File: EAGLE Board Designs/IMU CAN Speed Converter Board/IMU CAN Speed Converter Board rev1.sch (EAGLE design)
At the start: 24 parts, among them J1 CONNECTOR-CAN_NF_S_RA_BLACK, J2 CONNECTOR-CAN_NF_S_RA_BLACK, J3 JUMPER_1X02_, J4 JUMPER_1X02_, U1 LM340, U2 TCAN1051HQV-Q1, U3 TCAN1051HQV-Q1

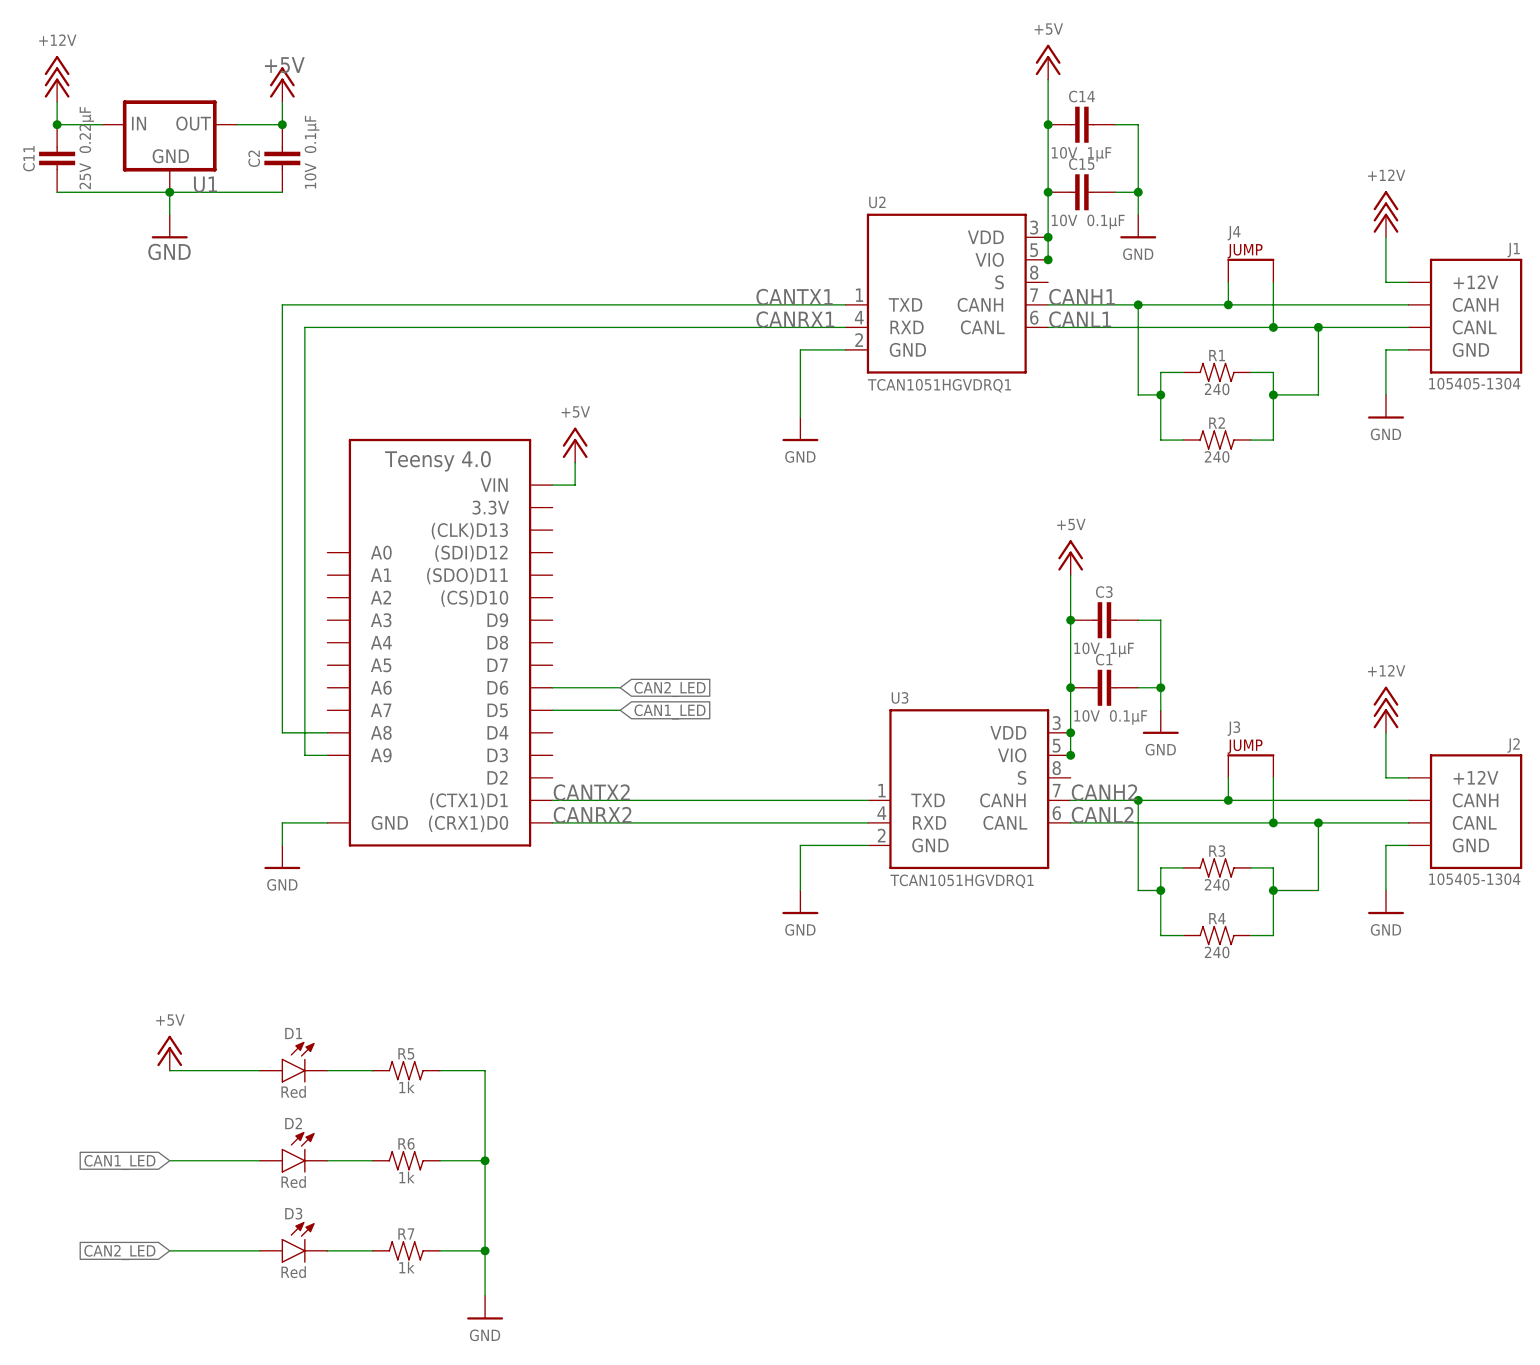
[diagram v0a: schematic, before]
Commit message: Update IMU CAN Speed Converter Board rev1.sch
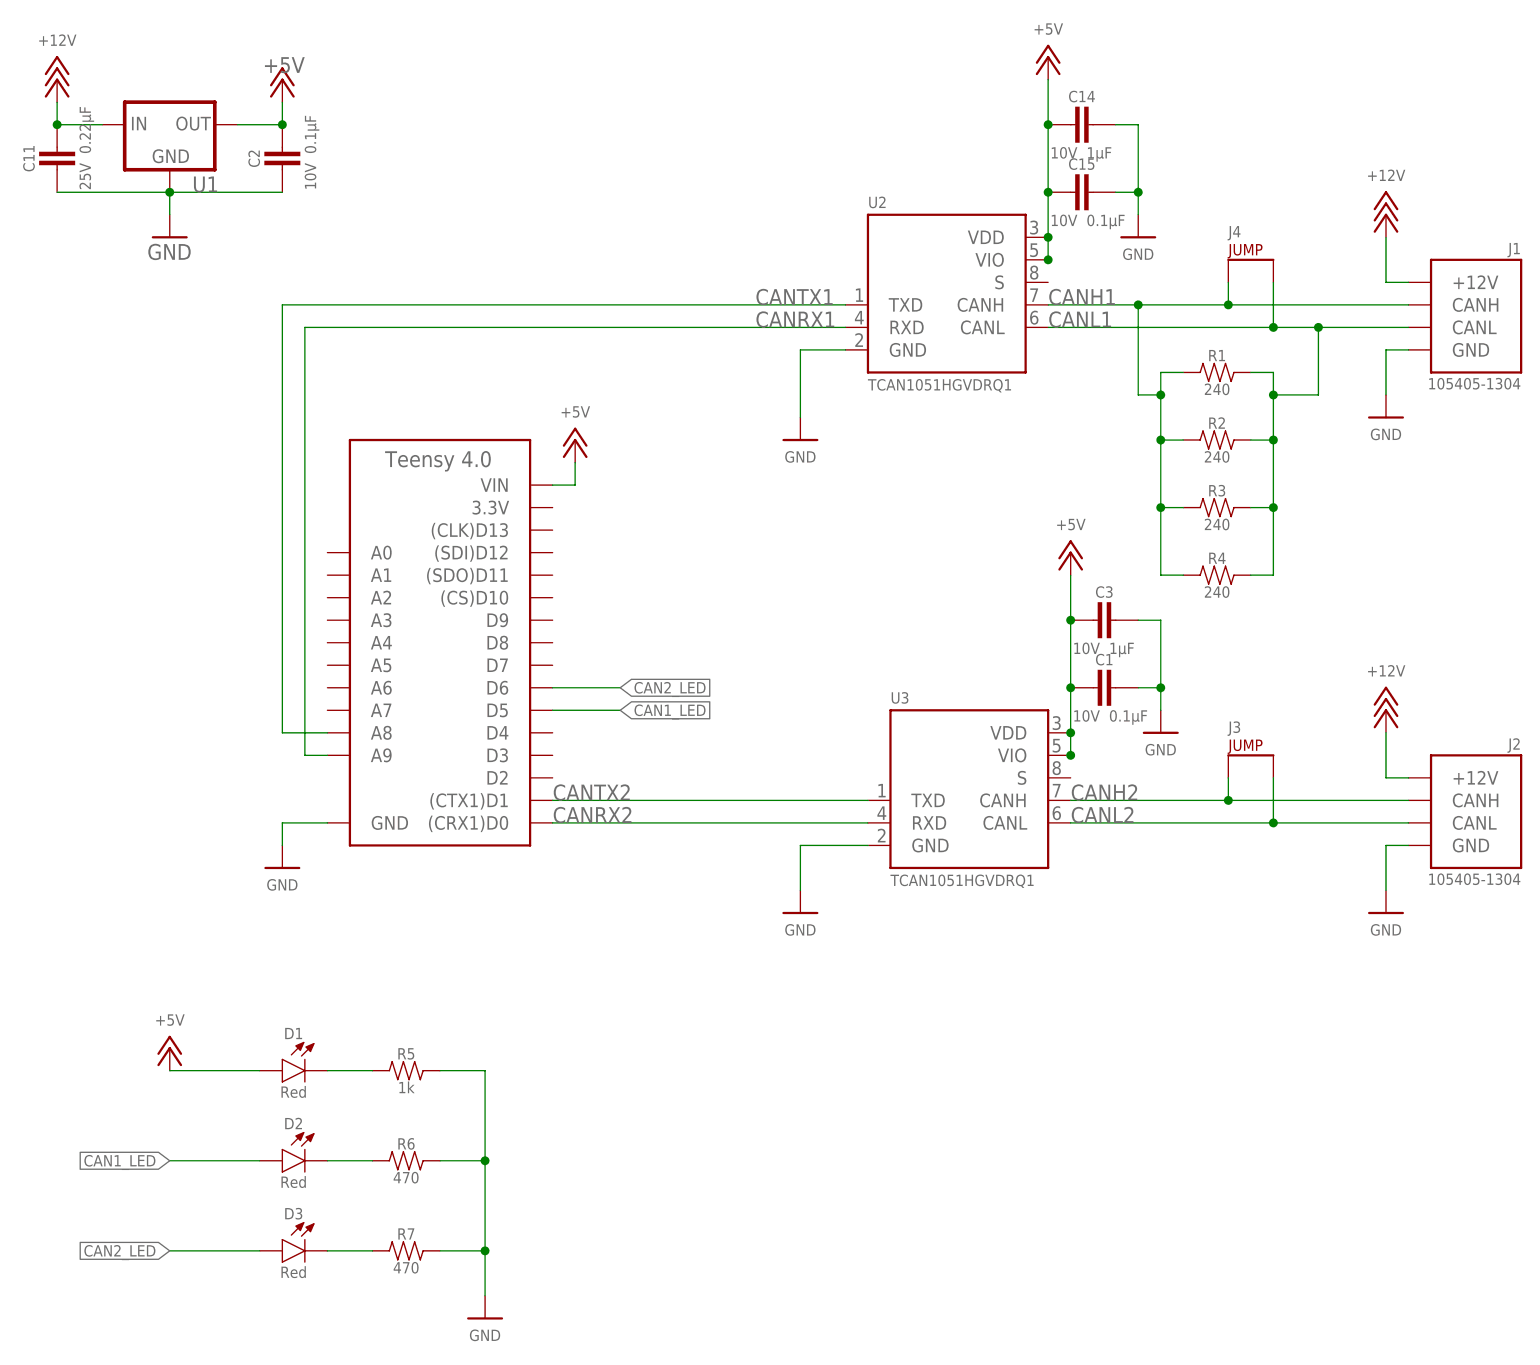
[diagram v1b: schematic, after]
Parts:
- R6, R7: value RESISTOR_0603_1K -> RESISTOR_0603_470; device HyTechDevices:RESISTOR_0603_1K -> HyTechDevices:RESISTOR_0603_470
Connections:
- net CANH1: now also R3.1, R4.1
- net CANH2: no longer R3.1, R4.1
- net CANL1: now also R3.2, R4.2
- net CANL2: no longer R3.2, R4.2
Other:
- moved on the sheet: R3, R4
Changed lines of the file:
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@@
 <part name="R1" library="HyTechDevices" deviceset="RESISTOR_?_*" device="0603" technology="240"/>
 <part name="R2" library="HyTechDevices" deviceset="RESISTOR_?_*" device="0603" technology="240"/>
-<part name="R3" library="HyTechDevices" deviceset="RESISTOR_?_*" device="0603" technology="240"/>
-<part name="R4" library="HyTechDevices" deviceset="RESISTOR_?_*" device="0603" technology="240"/>
 <part name="J3" library="HyTechDevices" deviceset="JUMPER_?_*" device="1X02"/>
 <part name="J4" library="HyTechDevices" deviceset="JUMPER_?_*" device="1X02"/>
 <part name="R5" library="HyTechDevices" deviceset="RESISTOR_?_*" device="0603" technology="1K"/>
-<part name="R6" library="HyTechDevices" deviceset="RESISTOR_?_*" device="0603" technology="1K"/>
-<part name="R7" library="HyTechDevices" deviceset="RESISTOR_?_*" device="0603" technology="1K"/>
+<part name="R6" library="HyTechDevices" deviceset="RESISTOR_?_*" device="0603" technology="470" value="RESISTOR_0603_470"/>
+<part name="R7" library="HyTechDevices" deviceset="RESISTOR_?_*" device="0603" technology="470" value="RESISTOR_0603_470"/>
 <part name="D1" library="HyTechDevices" deviceset="LED_?_*" device="0603" technology="RED"/>
 <part name="D2" library="HyTechDevices" deviceset="LED_?_*" device="0603" technology="RED"/>
@@
 <part name="P9" library="HyTechSupplies" deviceset="GND" device=""/>
 <part name="P10" library="HyTechSupplies" deviceset="+5V" device=""/>
+<part name="R3" library="HyTechDevices" deviceset="RESISTOR_?_*" device="0603" technology="240"/>
+<part name="R4" library="HyTechDevices" deviceset="RESISTOR_?_*" device="0603" technology="240"/>
 </parts>
 <sheets>
@@
 <attribute name="RESISTANCE" x="156.21" y="135.89" size="1.27" layer="96" align="top-center"/>
 </instance>
-<instance part="R3" gate="G$1" x="157.48" y="88.9" smashed="yes">
-<attribute name="NAME" x="156.21" y="90.17" size="1.27" layer="95" align="bottom-center"/>
-<attribute name="RESISTANCE" x="156.21" y="87.63" size="1.27" layer="96" align="top-center"/>
-</instance>
-<instance part="R4" gate="G$1" x="157.48" y="81.28" smashed="yes">
-<attribute name="NAME" x="156.21" y="82.55" size="1.27" layer="95" align="bottom-center"/>
-<attribute name="RESISTANCE" x="156.21" y="80.01" size="1.27" layer="96" align="top-center"/>
-</instance>
 <instance part="J3" gate="G$1" x="157.48" y="101.6" smashed="yes">
 <attribute name="NAME" x="157.48" y="104.14" size="1.27" layer="95"/>
@@
 <instance part="P10" gate="1" x="38.1" y="68.58" smashed="yes">
 <attribute name="VALUE" x="38.1" y="71.12" size="1.27" layer="96" align="bottom-center"/>
+</instance>
+<instance part="R3" gate="G$1" x="157.48" y="129.54" smashed="yes">
+<attribute name="NAME" x="156.21" y="130.81" size="1.27" layer="95" align="bottom-center"/>
+<attribute name="RESISTANCE" x="156.21" y="128.27" size="1.27" layer="96" align="top-center"/>
+</instance>
+<instance part="R4" gate="G$1" x="157.48" y="121.92" smashed="yes">
+<attribute name="NAME" x="156.21" y="123.19" size="1.27" layer="95" align="bottom-center"/>
+<attribute name="RESISTANCE" x="156.21" y="120.65" size="1.27" layer="96" align="top-center"/>
 </instance>
 </instances>
@@
 <wire x1="157.48" y1="154.94" x2="157.48" y2="152.4" width="0.1524" layer="91"/>
 <junction x="157.48" y="152.4"/>
+<wire x1="149.86" y1="137.16" x2="149.86" y2="129.54" width="0.1524" layer="91"/>
+<junction x="149.86" y="137.16"/>
+<pinref part="R3" gate="G$1" pin="1"/>
+<wire x1="149.86" y1="129.54" x2="152.4" y2="129.54" width="0.1524" layer="91"/>
+<wire x1="149.86" y1="129.54" x2="149.86" y2="121.92" width="0.1524" layer="91"/>
+<junction x="149.86" y="129.54"/>
+<pinref part="R4" gate="G$1" pin="1"/>
+<wire x1="149.86" y1="121.92" x2="152.4" y2="121.92" width="0.1524" layer="91"/>
 </segment>
 </net>
@@
 <wire x1="162.56" y1="154.94" x2="162.56" y2="149.86" width="0.1524" layer="91"/>
 <junction x="162.56" y="149.86"/>
+<wire x1="162.56" y1="137.16" x2="162.56" y2="129.54" width="0.1524" layer="91"/>
+<junction x="162.56" y="137.16"/>
+<pinref part="R3" gate="G$1" pin="2"/>
+<wire x1="162.56" y1="129.54" x2="160.02" y2="129.54" width="0.1524" layer="91"/>
+<wire x1="162.56" y1="129.54" x2="162.56" y2="121.92" width="0.1524" layer="91"/>
+<junction x="162.56" y="129.54"/>
+<pinref part="R4" gate="G$1" pin="2"/>
+<wire x1="162.56" y1="121.92" x2="160.02" y2="121.92" width="0.1524" layer="91"/>
 </segment>
 </net>
@@
 <pinref part="U3" gate="G$1" pin="CANH"/>
 <pinref part="J2" gate="G$1" pin="CANH"/>
-<wire x1="139.7" y1="96.52" x2="147.32" y2="96.52" width="0.1524" layer="91"/>
 <label x="139.7" y="96.52" size="1.778" layer="95"/>
-<pinref part="R3" gate="G$1" pin="1"/>
-<wire x1="147.32" y1="96.52" x2="157.48" y2="96.52" width="0.1524" layer="91"/>
+<wire x1="139.7" y1="96.52" x2="157.48" y2="96.52" width="0.1524" layer="91"/>
 <wire x1="157.48" y1="96.52" x2="177.8" y2="96.52" width="0.1524" layer="91"/>
-<wire x1="152.4" y1="88.9" x2="149.86" y2="88.9" width="0.1524" layer="91"/>
-<wire x1="149.86" y1="88.9" x2="149.86" y2="86.36" width="0.1524" layer="91"/>
-<pinref part="R4" gate="G$1" pin="1"/>
-<wire x1="149.86" y1="86.36" x2="149.86" y2="81.28" width="0.1524" layer="91"/>
-<wire x1="149.86" y1="81.28" x2="152.4" y2="81.28" width="0.1524" layer="91"/>
-<wire x1="149.86" y1="86.36" x2="147.32" y2="86.36" width="0.1524" layer="91"/>
-<junction x="149.86" y="86.36"/>
-<wire x1="147.32" y1="86.36" x2="147.32" y2="96.52" width="0.1524" layer="91"/>
-<junction x="147.32" y="96.52"/>
 <pinref part="J3" gate="G$1" pin="P$1"/>
 <wire x1="157.48" y1="99.06" x2="157.48" y2="96.52" width="0.1524" layer="91"/>
@@
 <wire x1="139.7" y1="93.98" x2="162.56" y2="93.98" width="0.1524" layer="91"/>
 <label x="139.7" y="93.98" size="1.778" layer="95"/>
-<pinref part="R3" gate="G$1" pin="2"/>
-<wire x1="162.56" y1="93.98" x2="167.64" y2="93.98" width="0.1524" layer="91"/>
-<wire x1="167.64" y1="93.98" x2="177.8" y2="93.98" width="0.1524" layer="91"/>
-<wire x1="160.02" y1="88.9" x2="162.56" y2="88.9" width="0.1524" layer="91"/>
-<wire x1="162.56" y1="88.9" x2="162.56" y2="86.36" width="0.1524" layer="91"/>
-<pinref part="R4" gate="G$1" pin="2"/>
-<wire x1="162.56" y1="86.36" x2="162.56" y2="81.28" width="0.1524" layer="91"/>
-<wire x1="162.56" y1="81.28" x2="160.02" y2="81.28" width="0.1524" layer="91"/>
-<wire x1="162.56" y1="86.36" x2="167.64" y2="86.36" width="0.1524" layer="91"/>
-<junction x="162.56" y="86.36"/>
-<wire x1="167.64" y1="86.36" x2="167.64" y2="93.98" width="0.1524" layer="91"/>
-<junction x="167.64" y="93.98"/>
+<wire x1="162.56" y1="93.98" x2="177.8" y2="93.98" width="0.1524" layer="91"/>
 <pinref part="J3" gate="G$1" pin="P$2"/>
 <wire x1="162.56" y1="99.06" x2="162.56" y2="93.98" width="0.1524" layer="91"/>

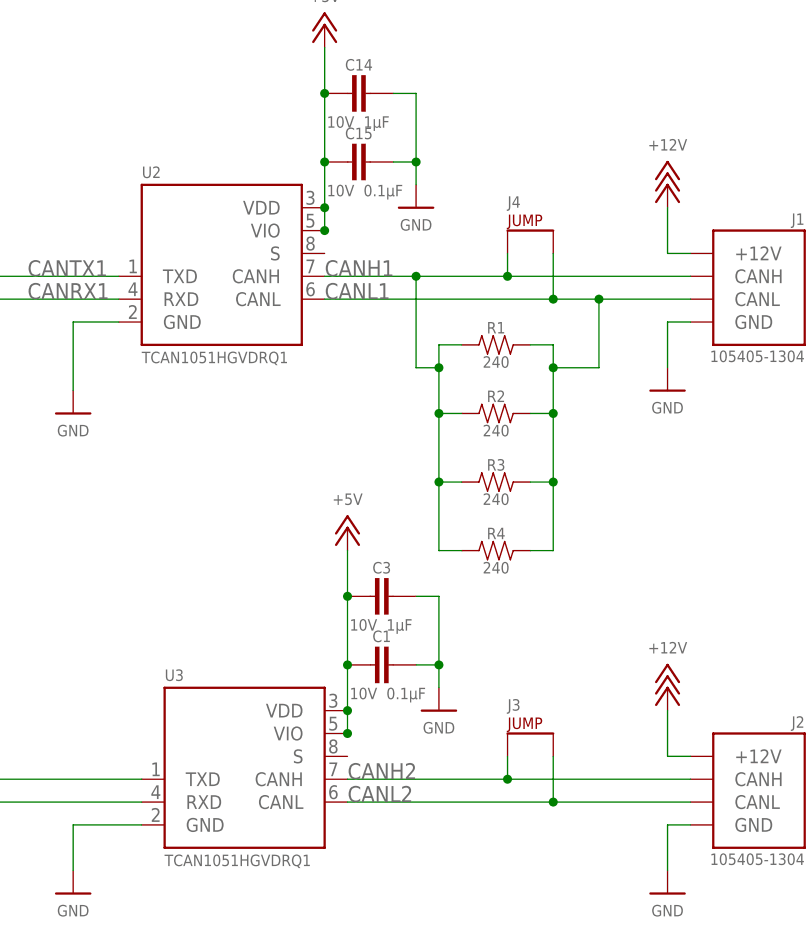
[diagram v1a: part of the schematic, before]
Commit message: Update IMU CAN Speed Converter Board rev1.sch
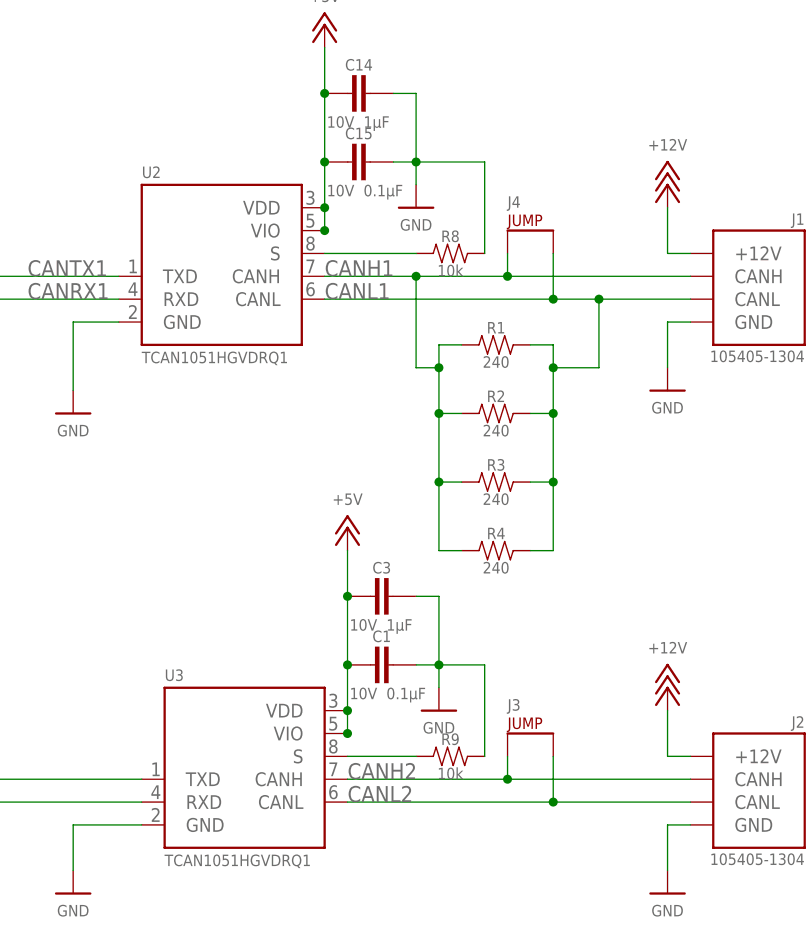
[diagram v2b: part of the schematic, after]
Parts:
- added R8, R9: RESISTOR_0603_10K, HyTechDevices:RESISTOR_0603_10K
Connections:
- new net N$4: R9.1, U3.S
- new net N$5: R8.1, U2.S
- net GND: now also R8.2, R9.2
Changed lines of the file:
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@@
 <part name="R3" library="HyTechDevices" deviceset="RESISTOR_?_*" device="0603" technology="240"/>
 <part name="R4" library="HyTechDevices" deviceset="RESISTOR_?_*" device="0603" technology="240"/>
+<part name="R8" library="HyTechDevices" deviceset="RESISTOR_?_*" device="0603" technology="10K"/>
+<part name="R9" library="HyTechDevices" deviceset="RESISTOR_?_*" device="0603" technology="10K"/>
 </parts>
 <sheets>
@@
 <attribute name="RESISTANCE" x="156.21" y="120.65" size="1.27" layer="96" align="top-center"/>
 </instance>
+<instance part="R8" gate="G$1" x="152.4" y="154.94" smashed="yes">
+<attribute name="NAME" x="151.13" y="156.21" size="1.27" layer="95" align="bottom-center"/>
+<attribute name="RESISTANCE" x="151.13" y="153.67" size="1.27" layer="96" align="top-center"/>
+</instance>
+<instance part="R9" gate="G$1" x="152.4" y="99.06" smashed="yes">
+<attribute name="NAME" x="151.13" y="100.33" size="1.27" layer="95" align="bottom-center"/>
+<attribute name="RESISTANCE" x="151.13" y="97.79" size="1.27" layer="96" align="top-center"/>
+</instance>
 </instances>
 <busses>
@@
 <wire x1="147.32" y1="172.72" x2="147.32" y2="165.1" width="0.1524" layer="91"/>
 <junction x="147.32" y="165.1"/>
+<pinref part="R8" gate="G$1" pin="2"/>
+<wire x1="154.94" y1="154.94" x2="154.94" y2="165.1" width="0.1524" layer="91"/>
+<wire x1="154.94" y1="165.1" x2="147.32" y2="165.1" width="0.1524" layer="91"/>
 </segment>
 <segment>
@@
 <wire x1="149.86" y1="116.84" x2="149.86" y2="109.22" width="0.1524" layer="91"/>
 <junction x="149.86" y="109.22"/>
+<wire x1="149.86" y1="109.22" x2="154.94" y2="109.22" width="0.1524" layer="91"/>
+<pinref part="R9" gate="G$1" pin="2"/>
+<wire x1="154.94" y1="109.22" x2="154.94" y2="99.06" width="0.1524" layer="91"/>
 </segment>
 <segment>
@@
 </segment>
 </net>
+<net name="N$4" class="0">
+<segment>
+<pinref part="U3" gate="G$1" pin="S"/>
+<pinref part="R9" gate="G$1" pin="1"/>
+<wire x1="139.7" y1="99.06" x2="147.32" y2="99.06" width="0.1524" layer="91"/>
+</segment>
+</net>
+<net name="N$5" class="0">
+<segment>
+<pinref part="U2" gate="G$1" pin="S"/>
+<pinref part="R8" gate="G$1" pin="1"/>
+<wire x1="137.16" y1="154.94" x2="147.32" y2="154.94" width="0.1524" layer="91"/>
+</segment>
+</net>
